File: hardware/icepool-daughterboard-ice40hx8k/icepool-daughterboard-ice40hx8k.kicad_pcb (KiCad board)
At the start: 4 copper layers, 21 x 32 mm, 33 parts, among them J20 Conn_02x08_Odd_Even, U7 AP7361C_SOT-89-5, U8 iCE40HX8K-BG121(121-Ball_caBG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, X2 ASEM1-12.000MHZ

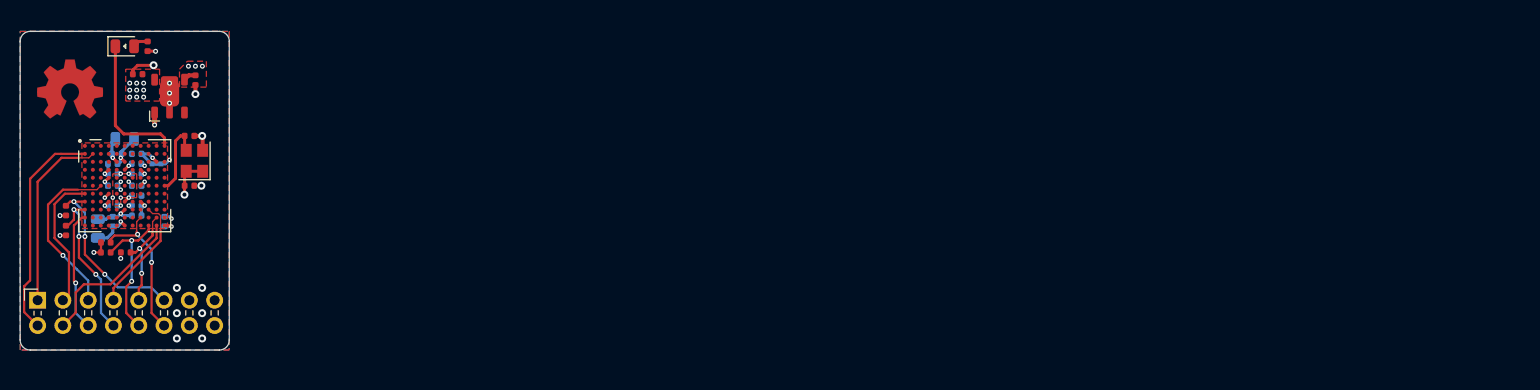
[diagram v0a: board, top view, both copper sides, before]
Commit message: New basis for icepool daughterboard.
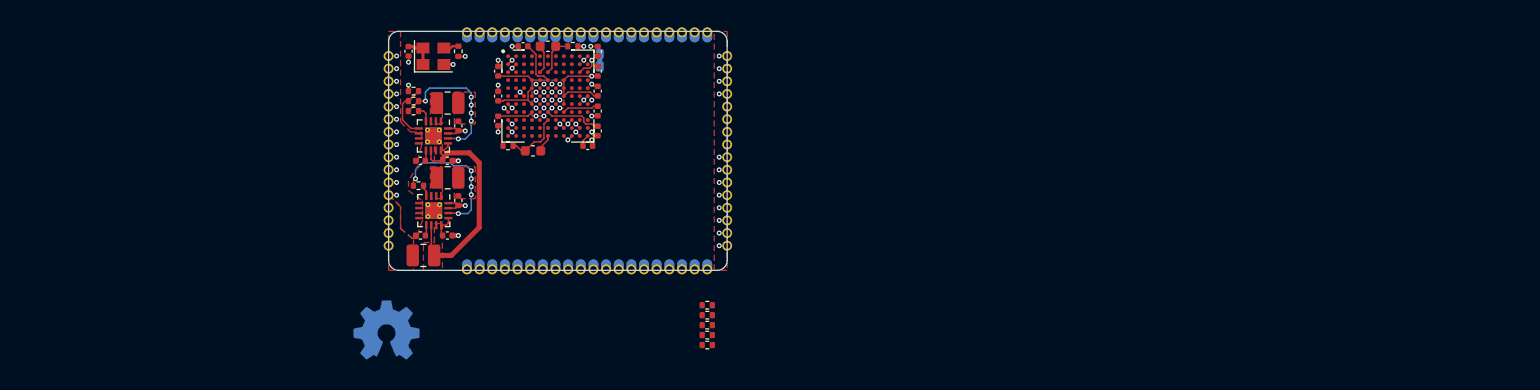
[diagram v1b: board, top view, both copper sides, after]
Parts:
- removed C16, C32, C36: 0.1u, Capacitor_SMD:C_0402_1005Metric
- removed C17: DNP, Capacitor_SMD:C_0402_1005Metric
- removed C21, C22: 4.7u, Capacitor_SMD:C_0402_1005Metric
- removed D2: LED_IND, LED_SMD:LED_0805_2012Metric
- removed J20: Conn_02x08_Odd_Even, Connector_PinSocket_2.54mm:PinSocket_2x08_P2.54mm_Horizontal
- removed R14: 1k, Resistor_SMD:R_0402_1005Metric
- removed U7: AP7361C_SOT-89-5, jkiv-library:SOT89-5
- removed X2: ASEM1-12.000MHZ, Oscillator:Oscillator_SMD_Abracon_ASE-4Pin_3.2x2.5mm
- added C1: 22u, Capacitor_SMD:C_0402_1005Metric, F.Cu at (70.0, 84.0)
- added C2: 10u, Capacitor_SMD:C_0402_1005Metric, F.Cu at (73.9, 102.5)
- added C3: 3.3n, Capacitor_SMD:C_0402_1005Metric, F.Cu at (71.2, 102.5)
- added C4: 22u, Capacitor_SMD:C_0402_1005Metric, F.Cu at (75.0, 99.0)
- added C5: 10u, Capacitor_SMD:C_0402_1005Metric, F.Cu at (73.9, 95.0)
- added C6: 3.3n, Capacitor_SMD:C_0402_1005Metric, F.Cu at (71.2, 95.0)
- added C7: 22u, Capacitor_SMD:C_0402_1005Metric, F.Cu at (75.0, 91.5)
- added J1: S, Connector_PinHeader_1.27mm:PinHeader_1x20_P1.27mm_Vertical, F.Cu at (75.9, 105.9)
- added J2: E, Connector_PinHeader_1.27mm:PinHeader_1x16_P1.27mm_Vertical, F.Cu at (102.0, 103.5)
- added J3: N, Connector_PinHeader_1.27mm:PinHeader_1x20_P1.27mm_Vertical, F.Cu at (100.0, 82.1)
- added J4: W, Connector_PinHeader_1.27mm:PinHeader_1x16_P1.27mm_Vertical, F.Cu at (68.0, 84.5)
- added L1: FB, Inductor_SMD:L_1008_2520Metric, F.Cu at (71.5, 104.5)
- added L2: 2.2u, Inductor_SMD:L_1008_2520Metric, F.Cu at (73.9, 96.7)
- added L3: 2.2u, Inductor_SMD:L_1008_2520Metric, F.Cu at (73.9, 89.2)
- added R1: 22R, Resistor_SMD:R_0402_1005Metric, F.Cu at (75.0, 84.0)
- added R2: 100k, Resistor_SMD:R_0402_1005Metric, F.Cu at (71.0, 97.5)
- added R3: 100k, Resistor_SMD:R_0402_1005Metric, F.Cu at (70.5, 90.0)
- added R4: 75k, Resistor_SMD:R_0402_1005Metric, F.Cu at (70.5, 89.0)
- added R5: 150k, Resistor_SMD:R_0402_1005Metric, F.Cu at (70.5, 88.0)
- added U1: TPS62140, Package_DFN_QFN:VQFN-16-1EP_3x3mm_P0.5mm_EP1.68x1.68mm_ThermalVias, F.Cu at (72.5, 100.0)
- added U2: TPS62140, Package_DFN_QFN:VQFN-16-1EP_3x3mm_P0.5mm_EP1.68x1.68mm_ThermalVias, F.Cu at (72.5, 92.5)
- added X1: ASEM1-12.000MHZ, Oscillator:Oscillator_SMD_Abracon_ASE-4Pin_3.2x2.5mm, F.Cu at (72.5, 84.5)
- C23, C24, C25, C26, C27, C28, C29, C30, C33, C34, R15, R16: moved to F.Cu
- C31, C35: footprint Capacitor_SMD:C_0805_2012Metric -> Capacitor_SMD:C_0603_1608Metric; moved to F.Cu
- JP1: footprint Jumper:SolderJumper-2_P1.3mm_Bridged_Pad1.0x1.5mm -> jkiv-library:J_Small_NC
- OSHW1: moved to B.Cu
- moved R31 65.4 mm to (100.0, 111.5), turned to 0 degrees
- moved R19 65.3 mm to (100.0, 112.5), turned to 0 degrees
- moved R18 61.1 mm to (100.0, 113.5)
- moved R20 60.7 mm to (100.0, 109.5)
- moved R17 58.7 mm to (100.0, 110.5)
- moved C33 49.6 mm to (89.0, 90.0), turned to 90 degrees
- moved C34 49.0 mm to (89.0, 92.0), turned to 90 degrees
- moved C29 48.2 mm to (89.0, 86.0), turned to 270 degrees
- moved R16 47.7 mm to (86.5, 83.5), turned to 0 degrees
- moved C26 47.4 mm to (89.0, 84.0), turned to 270 degrees
- moved C28 47.3 mm to (89.0, 88.0), turned to 270 degrees
- moved JP1 45.7 mm to (89.2, 84.9), turned to 90 degrees
- moved C31 44.4 mm to (82.5, 94.0), turned to 0 degrees
- moved C35 43.5 mm to (84.0, 83.5)
- moved U8 43.4 mm to (84.0, 88.5)
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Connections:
- net /ice40hx8k-daughter-board/CDONE renamed /CDONE
- net /ice40hx8k-daughter-board/CRESET_B renamed /CRESET_B
- net /ice40hx8k-daughter-board/ice40-hx8k-bg121/GNDPLL0 renamed /ice40-hx8k-bg121/GNDPLL0
- net /ice40hx8k-daughter-board/ice40-hx8k-bg121/GNDPLL1 renamed /ice40-hx8k-bg121/GNDPLL1
- net /ice40hx8k-daughter-board/ice40-hx8k-bg121/SDO0 renamed /ice40-hx8k-bg121/SDO0
- net /ice40hx8k-daughter-board/ice40-hx8k-bg121/VCCPLL0 renamed /ice40-hx8k-bg121/VCCPLL0
- net /ice40hx8k-daughter-board/ice40-hx8k-bg121/VCCPLL1 renamed /ice40-hx8k-bg121/VCCPLL1
- net /ice40hx8k-daughter-board/ice40-hx8k-bg121/VPP_2V5 renamed /ice40-hx8k-bg121/VPP_2V5
- net /ice40hx8k-daughter-board/~CS0 renamed /~CS0
- net /ice40hx8k-daughter-board/~CS1 renamed /~CS1
- net /ice40hx8k-daughter-board/~RESET renamed /~RESET
- U8 pad A11: /ice40hx8k-daughter-board/~LED -> /~LED
- U8 pad B1: /ice40hx8k-daughter-board/~READY_IN -> /~READY_IN
- U8 pad B2: /ice40hx8k-daughter-board/~READY_OUT -> /~READY_OUT
- U8 pad F11: /ice40hx8k-daughter-board/CLK_FPGA -> /OSC_12M
- U8 pad F3: /ice40hx8k-daughter-board/SDI1 -> /SDI1
- U8 pad G1: /ice40hx8k-daughter-board/SCK1 -> /SCK1
- U8 pad J9: /ice40hx8k-daughter-board/SDI0 -> /SDI0
- U8 pad K1: /ice40hx8k-daughter-board/SDO1 -> /SDO1
- U8 pad L10: /ice40hx8k-daughter-board/SCK0 -> /SCK0
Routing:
- net +12V: track 0.00 -> 25.6 mm
- net /ice40hx8k-daughter-board/~READY_IN: track 22.1 -> 0.00 mm
- net +3V3: track 17.5 -> 37.8 mm, vias 16 -> 6
- net /ice40hx8k-daughter-board/~READY_OUT: track 18.6 -> 0.00 mm
- net /ice40hx8k-daughter-board/SDI1: track 18.1 -> 0.00 mm, vias 1 -> 0
- net /~CS1: track 17.8 -> 0.57 mm, vias 3 -> 1
- net /~RESET: track 16.4 -> 0.57 mm, vias 3 -> 1
- net /ice40hx8k-daughter-board/SCK0: track 15.5 -> 0.00 mm
- net /CDONE: track 15.4 -> 0.57 mm, vias 2 -> 1
- net /ice40hx8k-daughter-board/~LED: track 14.2 -> 0.00 mm
- net /ice40hx8k-daughter-board/SCK1: track 14.0 -> 0.00 mm
- net /CRESET_B: track 14.5 -> 0.57 mm, vias 2 -> 1
- net /ice40hx8k-daughter-board/SDO1: track 12.1 -> 0.00 mm, vias 1 -> 0
- net /ice40hx8k-daughter-board/SDI0: track 11.9 -> 0.00 mm
- net +1V2: track 40.9 -> 29.6 mm, vias 13 -> 8
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- added copper zone on F.Cu, net +12V
- added copper zone on F.Cu, net /SW_1v2
- added copper zone on F.Cu, net /SW_3v3
- added copper zone on F.Cu, net 12V_IN
- added copper zone on In2.Cu, net GND
- removed copper zone on In2.Cu, net +1V2
- removed copper zone on In2.Cu, net +3V3
- removed copper zone on B.Cu, net GND
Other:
- board size 21 x 32 mm -> 34 x 24 mm
- board text removed: "+2v5"
- board text removed: "icepool 2021.02 ice40hx8k fourside.io"

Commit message: Yet another rework in progress.
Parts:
- J3: footprint Connector_PinHeader_1.27mm:PinHeader_1x20_P1.27mm_Vertical -> Connector_PinHeader_1.27mm:PinHeader_1x08_P1.27mm_Vertical
- moved J3 15.2 mm to (84.8, 82.0)
- moved J1 0.10 mm to (75.9, 106.0)
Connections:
- J3 pad 1: /CRESET_B -> /~CS1
- J3 pad 3: /~RESET -> /SDO1
- J3 pad 5: /CDONE -> /SCK1
- J3 pad 7: /~CS0 -> /~READY_IN
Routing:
- net /~READY_OUT: track 0.57 -> 0.00 mm, vias 1 -> 0
- net /SCK1: track 0.57 -> 0.00 mm, vias 1 -> 0
- net /~RESET: track 0.57 -> 0.00 mm, vias 1 -> 0
- net /~READY_IN: track 0.57 -> 0.00 mm, vias 1 -> 0
- net /~CS1: track 0.57 -> 0.00 mm, vias 1 -> 0
- net /SDO1: track 0.57 -> 0.00 mm, vias 1 -> 0
- net /SDI1: track 0.57 -> 0.00 mm, vias 1 -> 0
- net GND: track 15.3 -> 15.2 mm, vias 59 -> 71

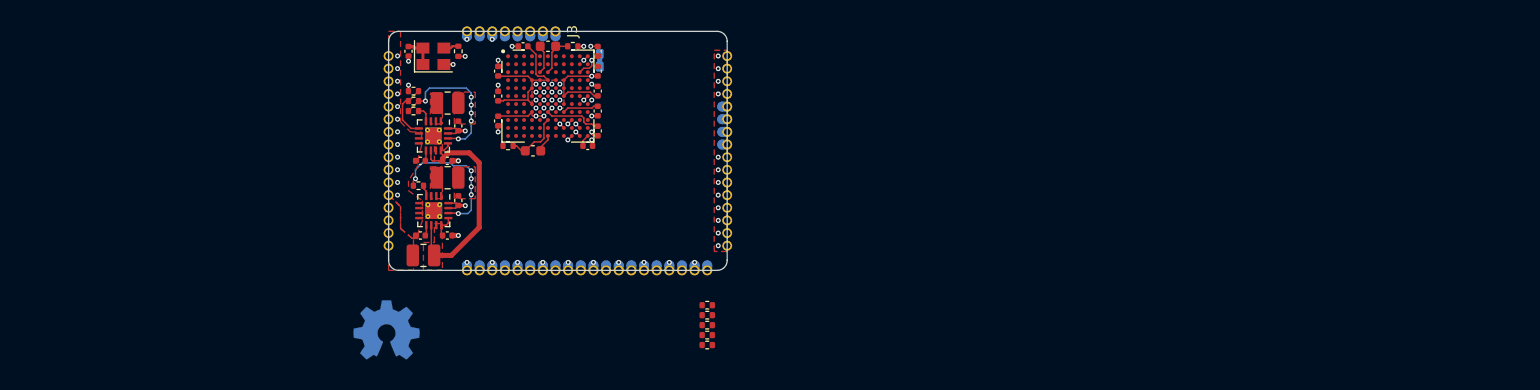
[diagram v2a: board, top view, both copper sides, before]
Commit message: SODIMM re-design + KiCad 6.
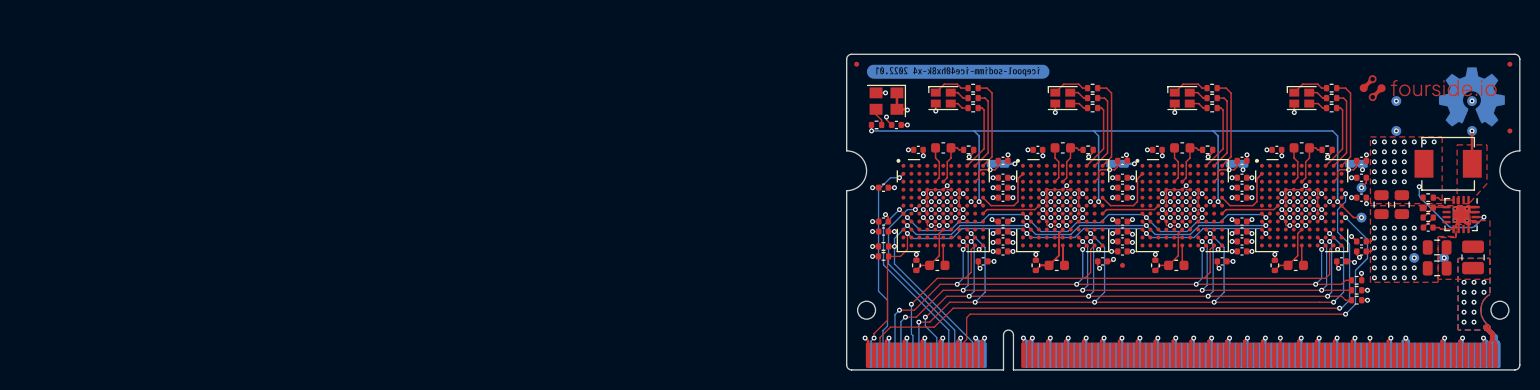
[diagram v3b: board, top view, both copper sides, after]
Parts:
- removed the C5 at (73.9, 95.0)
- removed the C6 at (71.2, 95.0)
- removed the C7 at (75.0, 91.5)
- removed J2: E, Connector_PinHeader_1.27mm:PinHeader_1x16_P1.27mm_Vertical
- removed J3: N, Connector_PinHeader_1.27mm:PinHeader_1x08_P1.27mm_Vertical
- removed J4: W, Connector_PinHeader_1.27mm:PinHeader_1x16_P1.27mm_Vertical
- removed L3: 2.2u, Inductor_SMD:L_1008_2520Metric
- removed R17, R18, R20: 10k, Resistor_SMD:R_0402_1005Metric
- removed the R4 at (70.5, 89.0)
- removed the R5 at (70.5, 88.0)
- added C1: DNP, Capacitor_SMD:C_0805_2012Metric, F.Cu at (173.3, 105.8)
- added C17: 0.1u, Capacitor_SMD:C_0402_1005Metric, F.Cu at (139.7, 105.1)
- added C18: 0.1u, Capacitor_SMD:C_0402_1005Metric, F.Cu at (129.7, 97.7)
- added C19: 0.1u, Capacitor_SMD:C_0402_1005Metric, F.Cu at (133.2, 93.9)
- added C20: 0.1u, Capacitor_SMD:C_0402_1005Metric, F.Cu at (141.7, 95.0)
- added C21: 0.1u, Capacitor_SMD:C_0402_1005Metric, F.Cu at (129.7, 102.1)
- added C22: 0.1u, Capacitor_SMD:C_0402_1005Metric, F.Cu at (141.7, 98.7)
- added C23: 0.1u, Capacitor_SMD:C_0402_1005Metric, F.Cu at (141.7, 96.7)
- added C24: 0.1u, Capacitor_SMD:C_0402_1005Metric, F.Cu at (129.7, 101.1)
- added C25: 10u, Capacitor_SMD:C_0603_1608Metric, F.Cu at (135.1, 105.5)
- added C26: 0.1u, Capacitor_SMD:C_0402_1005Metric, F.Cu at (141.7, 103.1)
- added C27: 0.1u, Capacitor_SMD:C_0402_1005Metric, F.Cu at (141.7, 104.1)
- added C28: 10u, Capacitor_SMD:C_0603_1608Metric, F.Cu at (135.7, 93.7)
- added C29: 0.1u, Capacitor_SMD:C_0402_1005Metric, F.Cu at (151.7, 105.1)
- added C30: 0.1u, Capacitor_SMD:C_0402_1005Metric, F.Cu at (141.7, 97.7)
- added C31: 0.1u, Capacitor_SMD:C_0402_1005Metric, F.Cu at (145.2, 93.9)
- added C32: 0.1u, Capacitor_SMD:C_0402_1005Metric, F.Cu at (153.7, 95.0)
- added C33: 0.1u, Capacitor_SMD:C_0402_1005Metric, F.Cu at (141.7, 102.1)
- added C34: 0.1u, Capacitor_SMD:C_0402_1005Metric, F.Cu at (153.7, 98.7)
- added C35: 0.1u, Capacitor_SMD:C_0402_1005Metric, F.Cu at (153.7, 96.7)
- added C36: 0.1u, Capacitor_SMD:C_0402_1005Metric, F.Cu at (141.7, 101.1)
- added C37: 10u, Capacitor_SMD:C_0603_1608Metric, F.Cu at (147.1, 105.5)
- added C38: 0.1u, Capacitor_SMD:C_0402_1005Metric, F.Cu at (153.7, 103.1)
- added C39: 0.1u, Capacitor_SMD:C_0402_1005Metric, F.Cu at (153.7, 104.1)
- added C40: 10u, Capacitor_SMD:C_0603_1608Metric, F.Cu at (147.7, 93.7)
- added C41: 0.1u, Capacitor_SMD:C_0402_1005Metric, F.Cu at (163.7, 105.1)
- added C42: 0.1u, Capacitor_SMD:C_0402_1005Metric, F.Cu at (153.7, 97.7)
- added C43: 0.1u, Capacitor_SMD:C_0402_1005Metric, F.Cu at (157.2, 93.9)
- added C44: 0.1u, Capacitor_SMD:C_0402_1005Metric, F.Cu at (165.7, 95.0)
- added C45: 0.1u, Capacitor_SMD:C_0402_1005Metric, F.Cu at (153.7, 102.1)
- added C46: 0.1u, Capacitor_SMD:C_0402_1005Metric, F.Cu at (165.7, 98.7)
- added C47: 0.1u, Capacitor_SMD:C_0402_1005Metric, F.Cu at (165.7, 96.7)
- added C48: 0.1u, Capacitor_SMD:C_0402_1005Metric, F.Cu at (153.7, 101.1)
- added C49: 10u, Capacitor_SMD:C_0603_1608Metric, F.Cu at (159.1, 105.5)
- added C50: 0.1u, Capacitor_SMD:C_0402_1005Metric, F.Cu at (165.7, 103.1)
- added C51: 0.1u, Capacitor_SMD:C_0402_1005Metric, F.Cu at (165.7, 104.1)
- added C52: 10u, Capacitor_SMD:C_0603_1608Metric, F.Cu at (159.7, 93.7)
- added C53: DNP, Capacitor_SMD:C_0805_2012Metric, F.Cu at (167.7, 99.4)
- added D1: ACT_LED, LED_SMD:LED_Cree-PLCC4_2x2mm_CW, F.Cu at (123.7, 88.7)
- added D2: ACT_LED, LED_SMD:LED_Cree-PLCC4_2x2mm_CW, F.Cu at (135.7, 88.7)
- added D3: ACT_LED, LED_SMD:LED_Cree-PLCC4_2x2mm_CW, F.Cu at (147.7, 88.7)
- added D4: ACT_LED, LED_SMD:LED_Cree-PLCC4_2x2mm_CW, F.Cu at (159.7, 88.7)
- added FID1: Fiducial, Fiducial:Fiducial_0.5mm_Mask1mm, F.Cu at (115.0, 85.3)
- added FID2: Fiducial, Fiducial:Fiducial_0.5mm_Mask1mm, F.Cu at (180.6, 85.3)
- added FID3: Fiducial, Fiducial:Fiducial_0.5mm_Mask1mm, F.Cu at (141.7, 105.5)
- added FID4: Fiducial, Fiducial:Fiducial_0.5mm_Mask1mm, F.Cu at (180.6, 92.0)
- added G***: LOGO, LOGO, F.Cu at (172.4, 87.7)
- added JP2: CUT_2V5, jkiv-library:J_Small_NC, B.Cu at (141.2, 95.3)
- added JP3: CUT_2V5, jkiv-library:J_Small_NC, B.Cu at (153.2, 95.3)
- added JP4: CUT_2V5, jkiv-library:J_Small_NC, B.Cu at (165.2, 95.3)
- added R1: 100k, Resistor_SMD:R_0402_1005Metric, F.Cu at (172.4, 98.7)
- added R10: 10k, Resistor_SMD:R_0402_1005Metric, F.Cu at (165.2, 108.0)
- added R11: 1k, Resistor_SMD:R_0402_1005Metric, F.Cu at (126.7, 88.7)
- added R12: 10k, Resistor_SMD:R_0402_1005Metric, F.Cu at (117.7, 103.6)
- added R13: 1k, Resistor_SMD:R_0402_1005Metric, F.Cu at (126.7, 89.7)
- added R14: 10k, Resistor_SMD:R_0402_1005Metric, F.Cu at (165.2, 109.0)
- added R15: 100R, Resistor_SMD:R_0402_1005Metric, F.Cu at (133.0, 105.5)
- added R16: 100R, Resistor_SMD:R_0402_1005Metric, F.Cu at (138.2, 93.9)
- added R21: 1k, Resistor_SMD:R_0402_1005Metric, F.Cu at (138.7, 88.7)
- added R23: 1k, Resistor_SMD:R_0402_1005Metric, F.Cu at (138.7, 89.7)
- added R25: 100R, Resistor_SMD:R_0402_1005Metric, F.Cu at (145.0, 105.5)
- added R26: 100R, Resistor_SMD:R_0402_1005Metric, F.Cu at (150.2, 93.9)
- added R29: 1k, Resistor_SMD:R_0402_1005Metric, F.Cu at (150.7, 87.7)
- added R33: 1k, Resistor_SMD:R_0402_1005Metric, F.Cu at (150.7, 89.7)
- added R35: 100R, Resistor_SMD:R_0402_1005Metric, F.Cu at (157.0, 105.5)
- added R36: 100R, Resistor_SMD:R_0402_1005Metric, F.Cu at (162.2, 93.9)
- added R39: 1k, Resistor_SMD:R_0402_1005Metric, F.Cu at (162.7, 87.7)
- added R41: 1k, Resistor_SMD:R_0402_1005Metric, F.Cu at (162.7, 88.7)
- added R43: 1k, Resistor_SMD:R_0402_1005Metric, F.Cu at (162.7, 89.7)
- added R7: 10k, Resistor_SMD:R_0402_1005Metric, F.Cu at (165.2, 107.0)
- added R8: 10k, Resistor_SMD:R_0402_1005Metric, F.Cu at (117.7, 104.6)
- added R9: 1k, Resistor_SMD:R_0402_1005Metric, F.Cu at (126.7, 87.7)
- added TP1: SW_1v2, TestPoint:TestPoint_Pad_D1.0mm, B.Cu at (176.8, 92.0)
- added TP2: GND, TestPoint:TestPoint_Pad_D1.0mm, B.Cu at (176.8, 89.0)
- added TP3: +12V, TestPoint:TestPoint_Pad_D1.0mm, B.Cu at (174.0, 104.8)
- added TP4: GND, TestPoint:TestPoint_Pad_D1.0mm, B.Cu at (171.0, 104.8)
- added TP5: +1v2, TestPoint:TestPoint_Pad_D1.0mm, B.Cu at (169.2, 92.0)
- added TP6: GND, TestPoint:TestPoint_Pad_D1.0mm, B.Cu at (169.2, 89.0)
- added TP7: OSC_CORE, TestPoint:TestPoint_Pad_D1.0mm, B.Cu at (165.7, 100.7)
- added TP8: GND, TestPoint:TestPoint_Pad_D1.0mm, B.Cu at (165.7, 97.7)
- added U3: iCE40HX8K-BG121(121-Ball_caBGA), jkiv-library:BGA-121_11x11_9.0x9.0mm, F.Cu at (159.7, 99.5)
- added U4: TPS62140, Package_DFN_QFN:VQFN-16-1EP_3x3mm_P0.5mm_EP1.68x1.68mm_ThermalVias, F.Cu at (175.7, 100.4)
- added kibuzzard-62B88C8F: G***, kibuzzard-62B88C8F, B.Cu at (178.5, 92.0)
- added kibuzzard-62B88CC0: G***, kibuzzard-62B88CC0, B.Cu at (167.6, 100.7)
- added kibuzzard-62B88D1E: G***, kibuzzard-62B88D1E, B.Cu at (171.5, 92.0)
- added kibuzzard-62B88D7B: G***, kibuzzard-62B88D7B, B.Cu at (176.1, 104.6)
- added kibuzzard-62C46161: G***, kibuzzard-62C46161, B.Cu at (125.2, 86.0)
- added kibuzzard-62C46174: G***, kibuzzard-62C46174, B.Cu at (125.2, 86.0)
- C2: value 10u -> 22u; footprint Capacitor_SMD:C_0402_1005Metric -> Capacitor_SMD:C_0805_2012Metric
- C4: footprint Capacitor_SMD:C_0402_1005Metric -> Capacitor_SMD:C_0805_2012Metric
- J1: value S -> SODIMM-200_Split; footprint Connector_PinHeader_1.27mm:PinHeader_1x20_P1.27mm_Vertical -> jkiv-library:SODIMM-200-DDR2-PCB
- L2: footprint Inductor_SMD:L_1008_2520Metric -> Inductor_SMD:L_Vishay_IHLP-2020
- R19, R31: value 10k -> 1k
- R2: value 100k -> 75k
- R3: value 100k -> 150k
- U1, U2: value TPS62140 -> iCE40HX8K-BG121(121-Ball_caBGA); footprint Package_DFN_QFN:VQFN-16-1EP_3x3mm_P0.5mm_EP1.68x1.68mm_ThermalVias -> jkiv-library:BGA-121_11x11_9.0x9.0mm
- moved OSHW1 111.5 mm to (176.8, 88.6)
- moved L1 105.4 mm to (176.9, 104.7), turned to 90 degrees
- moved R3 102.5 mm to (172.4, 100.7)
- moved R2 101.4 mm to (172.4, 99.7)
- moved C3 101.2 mm to (172.4, 101.7)
- moved L2 100.5 mm to (174.4, 95.3), turned to 180 degrees
- moved C2 99.4 mm to (173.3, 103.7)
- moved C4 94.8 mm to (169.8, 99.4)
- moved U2 75.5 mm to (147.7, 99.5), turned to 0 degrees
- moved U1 63.2 mm to (135.7, 99.5), turned to 0 degrees
- moved R31 55.6 mm to (150.7, 88.7), turned to 180 degrees
- moved C54 49.6 mm to (119.0, 91.4), turned to 0 degrees
- moved R19 46.0 mm to (138.7, 87.7), turned to 180 degrees
- moved X1 45.7 mm to (118.0, 89.0), turned to 180 degrees
- moved C14 42.8 mm to (129.7, 103.1), turned to 180 degrees
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- renumbered C28 to C10, C29 to C11, C30 to C12, C31 to C13, C33 to C14, C34 to C15, C35 to C16, C23 to C5, C1 to C54, C24 to C6, C25 to C7, C26 to C8, C27 to C9, R1 to R4, R15 to R5, R16 to R6, U8 to U0
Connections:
- net /ice40-hx8k-bg121/GNDPLL0 renamed /ice40hx8k 0/GNDPLL0
- net /ice40-hx8k-bg121/GNDPLL1 renamed /ice40hx8k 0/GNDPLL1
- net /ice40-hx8k-bg121/SDO0 renamed /ice40hx8k 0/SDO0
- net /ice40-hx8k-bg121/VCCPLL0 renamed /ice40hx8k 0/VCCPLL0
- net /ice40-hx8k-bg121/VCCPLL1 renamed /ice40hx8k 0/VCCPLL1
- net /ice40-hx8k-bg121/VPP_2V5 renamed /ice40hx8k 0/VPP_2V5
- C2 pad 1: +12V -> GND
- C2 pad 2: GND -> +12V
- C4 pad 1: +3V3 -> +1V2
- J1 pad 10: /SCK0 -> /CRESET_B
- J1 pad 11: GND -> unconnected-(J1-Pad11)
- J1 pad 12: /SDI0 -> /CDONE
- J1 pad 14: /~CS0 -> GND
- J1 pad 15: GND -> unconnected-(J1-Pad15)
- J1 pad 16: /CDONE -> /SCK0
- J1 pad 17: GND -> unconnected-(J1-Pad17)
- J1 pad 18: /~RESET -> /SDI0
- J1 pad 2: /~READY_OUT -> /~{RESET}
- J1 pad 20: /CRESET_B -> GND
- J1 pad 3: GND -> unconnected-(J1-Pad3)
- J1 pad 4: /SCK1 -> unconnected-(J1-Pad4)
- J1 pad 5: GND -> /~{READY_IN}
- J1 pad 6: /SDI1 -> /~{READY_OUT}
- J1 pad 8: /~CS1 -> GND
- J1 pad 9: GND -> unconnected-(J1-Pad9)
- L2 pad 1: /SW_3v3 -> /SW_1v2
- L2 pad 2: +3V3 -> +1V2
- R19 pad 1: +3V3 -> /ice40-hx8k 1/~{ACT_R}
- R19 pad 2: /~RESET -> Net-(D2-Pad1)
- R2 pad 1: +3V3 -> +1V2
- R3 pad 1: +1V2 -> Net-(R2-Pad2)
- R3 pad 2: Net-(R3-Pad2) -> GND
- R31 pad 1: +3V3 -> /ice40-hx8k 2/~{ACT_G}
- R31 pad 2: /~CS1 -> Net-(D3-Pad2)
- R4 pad 1: /OSC_12M -> /OSC_CORE
- U0 pad A1: Net-(U8-PadA1) -> unconnected-(U0-PadA1)
- U0 pad A10: Net-(U8-PadA10) -> /ice40hx8k 0/~{ACT_G}
- U0 pad A11: /~LED -> /ice40hx8k 0/~{ACT_R}
- U0 pad A2: Net-(U8-PadA2) -> unconnected-(U0-PadA2)
- U0 pad A3: Net-(U8-PadA3) -> unconnected-(U0-PadA3)
- U0 pad A4: Net-(U8-PadA4) -> unconnected-(U0-PadA4)
- U0 pad A5: Net-(U8-PadA5) -> unconnected-(U0-PadA5)
- U0 pad A6: Net-(U8-PadA6) -> unconnected-(U0-PadA6)
- U0 pad A7: Net-(U8-PadA7) -> unconnected-(U0-PadA7)
- U0 pad A8: Net-(U8-PadA8) -> unconnected-(U0-PadA8)
- U0 pad A9: Net-(U8-PadA9) -> /ice40hx8k 0/~{ACT_B}
- U0 pad B1: /~READY_IN -> /~{READY_OUT}
- U0 pad B10: Net-(U8-PadB10) -> unconnected-(U0-PadB10)
- U0 pad B11: Net-(U8-PadB11) -> unconnected-(U0-PadB11)
- U0 pad B2: /~READY_OUT -> unconnected-(U0-PadB2)
- U0 pad B3: Net-(U8-PadB3) -> unconnected-(U0-PadB3)
- U0 pad B4: Net-(U8-PadB4) -> unconnected-(U0-PadB4)
- U0 pad B5: Net-(U8-PadB5) -> unconnected-(U0-PadB5)
- U0 pad B6: Net-(U8-PadB6) -> unconnected-(U0-PadB6)
- U0 pad B7: Net-(U8-PadB7) -> unconnected-(U0-PadB7)
- U0 pad B8: Net-(U8-PadB8) -> unconnected-(U0-PadB8)
- U0 pad B9: Net-(U8-PadB9) -> unconnected-(U0-PadB9)
- U0 pad C1: Net-(U8-PadC1) -> unconnected-(U0-PadC1)
- U0 pad C11: Net-(U8-PadC11) -> unconnected-(U0-PadC11)
- U0 pad C2: Net-(U8-PadC2) -> unconnected-(U0-PadC2)
- U0 pad C3: Net-(U8-PadC3) -> unconnected-(U0-PadC3)
- U0 pad C4: Net-(U8-PadC4) -> unconnected-(U0-PadC4)
- U0 pad C7: Net-(U8-PadC7) -> unconnected-(U0-PadC7)
- U0 pad C8: Net-(U8-PadC8) -> unconnected-(U0-PadC8)
- U0 pad C9: Net-(U8-PadC9) -> unconnected-(U0-PadC9)
- U0 pad D1: Net-(U8-PadD1) -> unconnected-(U0-PadD1)
- U0 pad D10: Net-(U8-PadD10) -> unconnected-(U0-PadD10)
- U0 pad D11: Net-(U8-PadD11) -> unconnected-(U0-PadD11)
- U0 pad D2: Net-(U8-PadD2) -> unconnected-(U0-PadD2)
- U0 pad D3: Net-(U8-PadD3) -> unconnected-(U0-PadD3)
- U0 pad D5: Net-(U8-PadD5) -> unconnected-(U0-PadD5)
- U0 pad D7: Net-(U8-PadD7) -> unconnected-(U0-PadD7)
- U0 pad D9: Net-(U8-PadD9) -> unconnected-(U0-PadD9)
- U0 pad E1: Net-(U8-PadE1) -> unconnected-(U0-PadE1)
- U0 pad E10: Net-(U8-PadE10) -> unconnected-(U0-PadE10)
- U0 pad E11: Net-(U8-PadE11) -> /ice40-hx8k 1/~{READY_OUT}
- U0 pad E2: Net-(U8-PadE2) -> unconnected-(U0-PadE2)
- U0 pad E3: Net-(U8-PadE3) -> unconnected-(U0-PadE3)
- U0 pad E8: Net-(U8-PadE8) -> unconnected-(U0-PadE8)
- U0 pad E9: Net-(U8-PadE9) -> unconnected-(U0-PadE9)
- U0 pad F1: Net-(U8-PadF1) -> unconnected-(U0-PadF1)
- U0 pad F10: Net-(U8-PadF10) -> unconnected-(U0-PadF10)
- U0 pad F11: /OSC_12M -> /OSC_CORE
- U0 pad F2: Net-(U8-PadF2) -> unconnected-(U0-PadF2)
- U0 pad F4: Net-(U8-PadF4) -> unconnected-(U0-PadF4)
- U0 pad F9: Net-(U8-PadF9) -> unconnected-(U0-PadF9)
- U0 pad G10: Net-(U8-PadG10) -> unconnected-(U0-PadG10)
- U0 pad G11: Net-(U8-PadG11) -> /ice40-hx8k 1/SDI1
- U0 pad G2: Net-(U8-PadG2) -> unconnected-(U0-PadG2)
- U0 pad G3: Net-(U8-PadG3) -> unconnected-(U0-PadG3)
- U0 pad G8: Net-(U8-PadG8) -> unconnected-(U0-PadG8)
- U0 pad G9: Net-(U8-PadG9) -> unconnected-(U0-PadG9)
- U0 pad H1: /~CS1 -> /~{CS1}
- U0 pad H10: Net-(U8-PadH10) -> unconnected-(U0-PadH10)
- U0 pad H11: Net-(U8-PadH11) -> unconnected-(U0-PadH11)
- U0 pad H2: Net-(U8-PadH2) -> unconnected-(U0-PadH2)
- U0 pad H3: Net-(U8-PadH3) -> unconnected-(U0-PadH3)
- U0 pad H7: Net-(U8-PadH7) -> unconnected-(U0-PadH7)
- U0 pad H9: Net-(U8-PadH9) -> unconnected-(U0-PadH9)
- U0 pad J1: /~RESET -> /~{RESET}
- U0 pad J10: Net-(U8-PadJ10) -> unconnected-(U0-PadJ10)
- U0 pad J11: Net-(U8-PadJ11) -> unconnected-(U0-PadJ11)
- U0 pad J2: Net-(U8-PadJ2) -> unconnected-(U0-PadJ2)
- U0 pad J3: Net-(U8-PadJ3) -> unconnected-(U0-PadJ3)
- U0 pad J4: Net-(U8-PadJ4) -> unconnected-(U0-PadJ4)
- U0 pad J5: Net-(U8-PadJ5) -> unconnected-(U0-PadJ5)
- U0 pad J7: Net-(U8-PadJ7) -> unconnected-(U0-PadJ7)
- U0 pad J8: Net-(U8-PadJ8) -> unconnected-(U0-PadJ8)
- U0 pad K1: /SDO1 -> unconnected-(U0-PadK1)
- U0 pad K10: /~CS0 -> /~{CS0}
- U0 pad K11: Net-(U8-PadK11) -> unconnected-(U0-PadK11)
- U0 pad K2: Net-(U8-PadK2) -> unconnected-(U0-PadK2)
- U0 pad K3: Net-(U8-PadK3) -> unconnected-(U0-PadK3)
- U0 pad K4: Net-(U8-PadK4) -> unconnected-(U0-PadK4)
- U0 pad K5: Net-(U8-PadK5) -> unconnected-(U0-PadK5)
- U0 pad K6: Net-(U8-PadK6) -> unconnected-(U0-PadK6)
- U0 pad K7: Net-(U8-PadK7) -> unconnected-(U0-PadK7)
- U0 pad L1: Net-(U8-PadL1) -> unconnected-(U0-PadL1)
- U0 pad L2: Net-(U8-PadL2) -> unconnected-(U0-PadL2)
- U0 pad L3: Net-(U8-PadL3) -> unconnected-(U0-PadL3)
- U0 pad L4: Net-(U8-PadL4) -> unconnected-(U0-PadL4)
- U0 pad L5: Net-(U8-PadL5) -> unconnected-(U0-PadL5)
- U0 pad L7: Net-(U8-PadL7) -> unconnected-(U0-PadL7)
- U0 pad L8: Net-(U8-PadL8) -> unconnected-(U0-PadL8)
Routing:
- net GND: track 15.2 -> 141.2 mm, vias 71 -> 181
- net /OSC_CORE: track 0.00 -> 80.9 mm, vias 0 -> 6
- net /SDI0: track 0.57 -> 79.6 mm, vias 1 -> 9
- net /~{CS0}: track 0.00 -> 73.6 mm, vias 0 -> 9
- net /CDONE: track 0.57 -> 73.4 mm, vias 1 -> 9
- net /CRESET_B: track 0.57 -> 68.6 mm, vias 1 -> 9
- net /~{READY_IN}: track 0.00 -> 62.6 mm, vias 0 -> 2
- net /SCK0: track 0.57 -> 62.6 mm
- net /SCK1: track 0.00 -> 61.0 mm, vias 0 -> 5
- net /~{CS1}: track 0.00 -> 57.9 mm, vias 0 -> 5
- net /~{RESET}: track 0.00 -> 55.0 mm, vias 0 -> 5
- net /SDO1: track 0.00 -> 54.2 mm, vias 0 -> 2
- net +12V: track 25.6 -> 0.00 mm, vias 0 -> 1
- net /~{READY_OUT}: track 0.00 -> 20.3 mm, vias 0 -> 1
- net /SDI1: track 0.00 -> 19.5 mm, vias 0 -> 1
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- added copper zone on In2.Cu, net +1V2
- added copper zone on In3.Cu, net +3V3
- added copper zone on B.Cu, net 12V_IN
- added copper zone on In4.Cu, net GND
- removed copper zone on F.Cu, net +3V3
- removed copper zone on F.Cu, net /SW_3v3
- removed copper zone on In1.Cu, net GND
- removed copper zone on In2.Cu, net GND
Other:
- board size 34 x 24 mm -> 67.6 x 31.7 mm
- copper layers 4 -> 6
- net class Default removed
